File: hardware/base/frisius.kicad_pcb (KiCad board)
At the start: 4 copper layers, 46 x 85 mm, 123 parts, among them J1 MEM2067, J2 USB_C_Receptacle_USB2.0, J3 BATTERY, J4 Debug UART, J5 DISPLAY, J7 I2C ISENSE, Q2 Q_NMOS_DGS, Q3 Q_NMOS_DGS, SW1 RESET, SW2 BOOT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

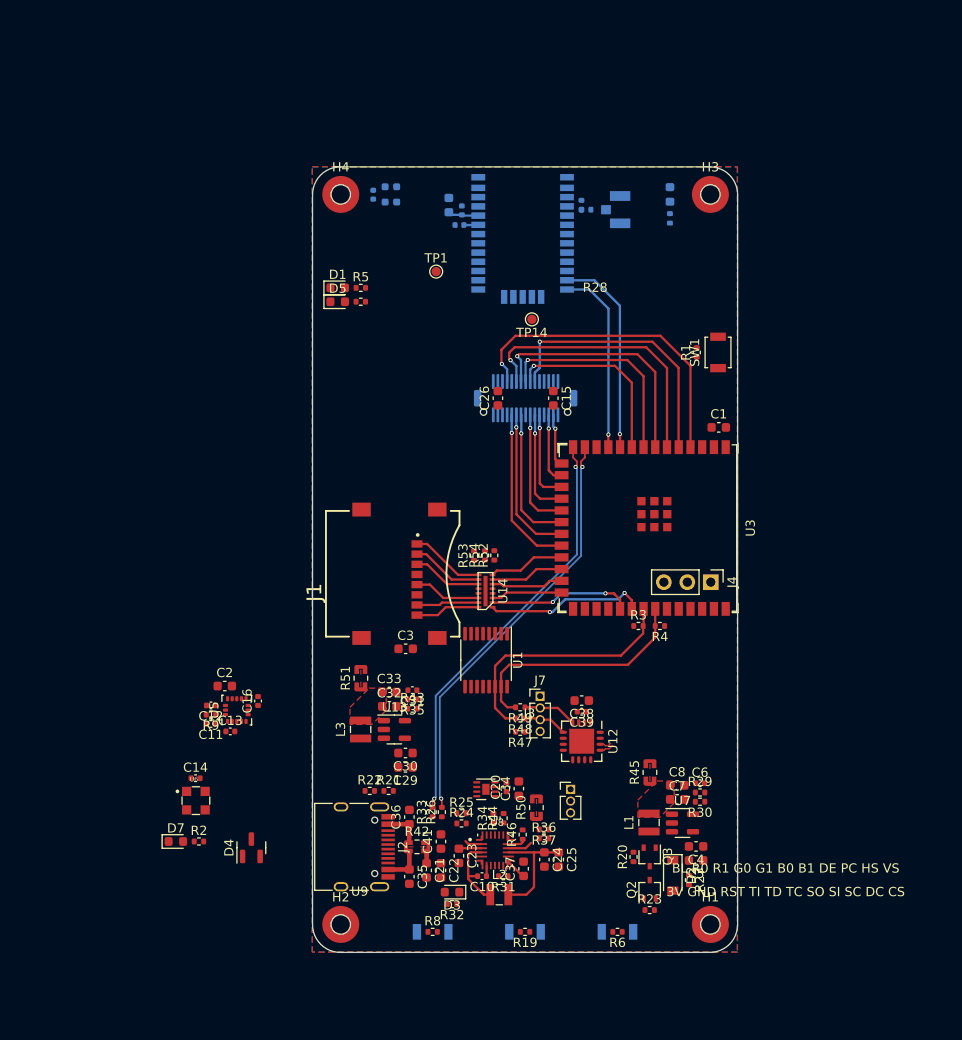
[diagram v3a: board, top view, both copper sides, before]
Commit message: more layout, optimising i2c
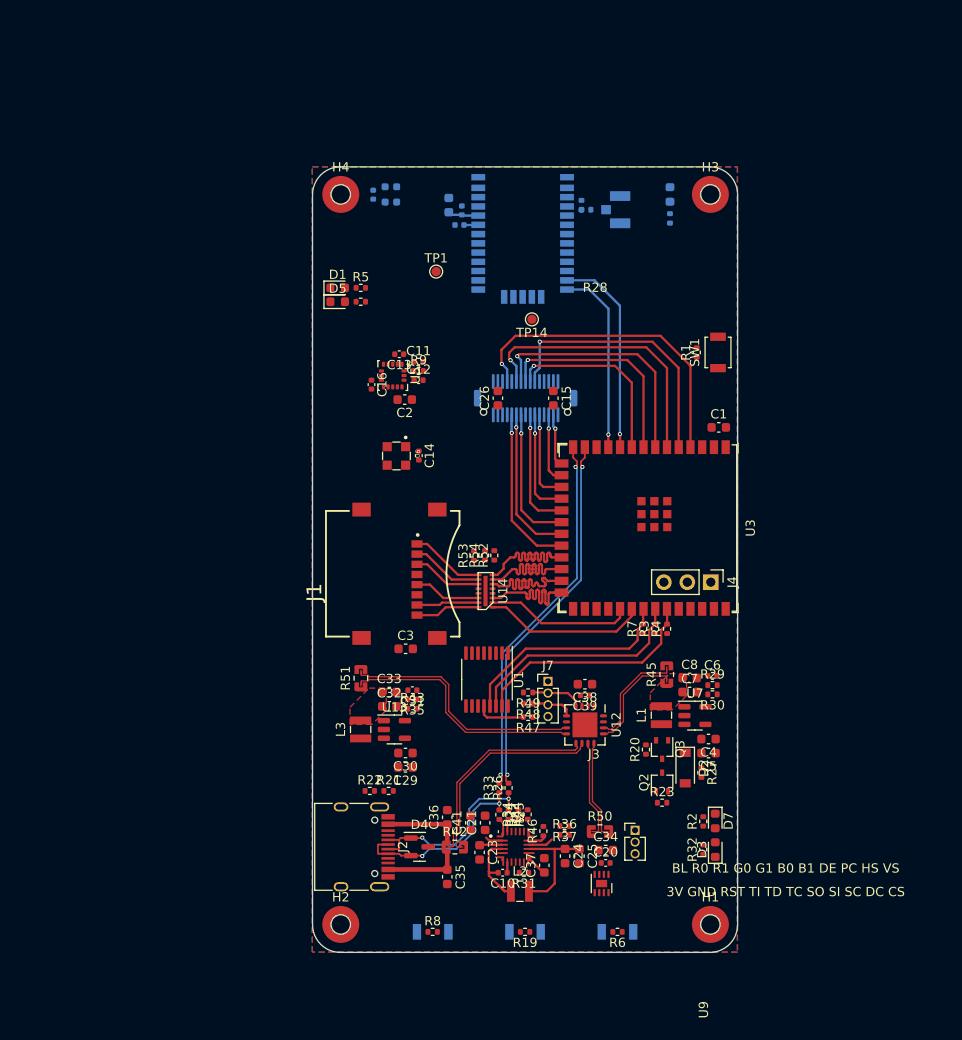
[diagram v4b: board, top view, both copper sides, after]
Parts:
- removed C22: 4.7u, Capacitor_SMD:C_0603_1608Metric
- added R7: 4.7k, Resistor_SMD:R_0402_1005Metric, F.Cu at (87.8, 95.0)
- moved D7 58.4 mm to (95.6, 115.8), turned to -90 degrees
- moved R2 54.6 mm to (94.3, 115.8), turned to 90 degrees
- moved C11 45.2 mm to (63.5, 66.1), turned to 0 degrees
- moved C13 44.7 mm to (61.4, 65.3), turned to 180 degrees
- moved R9 43.5 mm to (63.5, 67.1), turned to 0 degrees
- moved U6 43.2 mm to (61.1, 76.3), turned to -90 degrees
- moved C14 42.5 mm to (63.5, 76.3), turned to -90 degrees
- moved C12 41.8 mm to (63.5, 68.1), turned to 0 degrees
- moved U5 39.9 mm to (60.7, 67.6), turned to -90 degrees
- moved C2 36.6 mm to (62.0, 70.2), turned to 180 degrees
- moved C16 36.4 mm to (58.4, 68.6), turned to -90 degrees
- moved D3 28.9 mm to (95.6, 118.9), turned to 90 degrees
- moved R32 27.8 mm to (94.3, 118.9), turned to 90 degrees
- moved D4 18.2 mm to (63.6, 118.6), turned to 0 degrees
- moved U9 16.1 mm to (83.3, 122.6), turned to -90 degrees
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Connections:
- net Net-(C16-Pad1) renamed /Sensors/imu_crst
- net Net-(C35-Pad1) renamed /Power/vbus_port
- net Net-(D1-Pad2) renamed /GPS/1pps_led
- net Net-(D5-Pad2) renamed /GPS/3df_led
- net Net-(L1-Pad1) renamed /Power/core_drv
- net Net-(L3-Pad1) renamed /Power/aux_drv
- net Net-(R19-Pad1) renamed /Power/btn_nvdc
- C31 pad 1: Net-(C31-Pad1) -> /Power/aux_sw
- C32 pad 1: VDD_AUX_3V3 -> /Power/aux_sw
- C33 pad 1: VDD_AUX_3V3 -> /Power/aux_sw
- C6 pad 1: Net-(C6-Pad1) -> /Power/vcore_sw
- C7 pad 1: VDD_CORE_3V3 -> /Power/vcore_sw
- C8 pad 1: VDD_CORE_3V3 -> /Power/vcore_sw
- D4 pad 1: /Power/USB_D+ -> /Power/USB_D-
- D4 pad 2: /Power/USB_D- -> /Power/USB_D+
- L1 pad 2: Net-(C6-Pad1) -> /Power/vcore_sw
- L3 pad 2: Net-(C31-Pad1) -> /Power/aux_sw
- R29 pad 1: Net-(C6-Pad1) -> /Power/vcore_sw
- R35 pad 1: Net-(C31-Pad1) -> /Power/aux_sw
- R45 pad 1: Net-(C6-Pad1) -> /Power/vcore_sw
- R51 pad 1: Net-(C31-Pad1) -> /Power/aux_sw
- R51 pad 2: /Power/VAUX_S+ -> unconnected-(R51-Pad2)
- U1 pad 10: /Power/AUX_REG_EN -> /Power/BMS_INT
- U1 pad 9: /Power/BMS_INT -> /Power/AUX_REG_EN
- U12 pad 10: /Power/VBAT_S- -> /Power/VBUS_S-
- U12 pad 11: /Power/VCORE_S+ -> /Power/VBAT_S-
- U12 pad 12: /Power/VCORE_S- -> /Power/VBAT_S+
- U12 pad 13: /Power/VAUX_S+ -> /Power/VCORE_S+
- U12 pad 14: /Power/VAUX_S- -> /Power/VCORE_S-
- U12 pad 7: /Power/VBUS_S- -> /Power/VAUX_S-
- U12 pad 8: /Power/VBUS_S+ -> /Power/VAUX_S+
- U12 pad 9: /Power/VBAT_S+ -> /Power/VBUS_S+
- U3 pad 33: /Display/SYS_I2C.SDA -> /Processor/IOEXP_INT
- U3 pad 34: /Display/SYS_I2C.SCL -> /Display/SYS_I2C.SDA
- U3 pad 35: /Processor/IOEXP_INT -> /Display/SYS_I2C.SCL
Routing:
- net /Power/VAUX_S-: track 1.32 -> 26.8 mm
- net /Power/VAUX_S+: track 1.59 -> 26.8 mm
- net /Processor/IOEXP_INT: track 0.00 -> 24.1 mm
- net /Power/VBUS_S-: track 0.00 -> 22.8 mm
- net /Power/VBUS_S+: track 0.00 -> 22.8 mm
- net /Power/USB_D-: track 0.00 -> 20.9 mm, vias 0 -> 2
- net /Power/USB_D+: track 0.00 -> 20.9 mm, vias 0 -> 2
- net /Power/VCORE_S+: track 0.00 -> 11.6 mm
- net /Power/VCORE_S-: track 0.00 -> 11.6 mm
- net /Power/VBAT_S-: track 0.00 -> 10.5 mm
- net /Power/VBAT_S+: track 0.00 -> 10.5 mm
- net /Processor/SDMMC.D2: track 7.94 -> 16.2 mm
- net /Processor/SDMMC.CLK: track 7.71 -> 16.0 mm
- net /Power/vbus_port: track 8.59 -> 16.8 mm
- net /Processor/SDMMC.D3: track 8.25 -> 16.4 mm
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- added copper zone on F.Cu, net /Power/vcore_sw

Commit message: layout complete, drc checks and tweaks to silkscreen, attempting geo reannotate
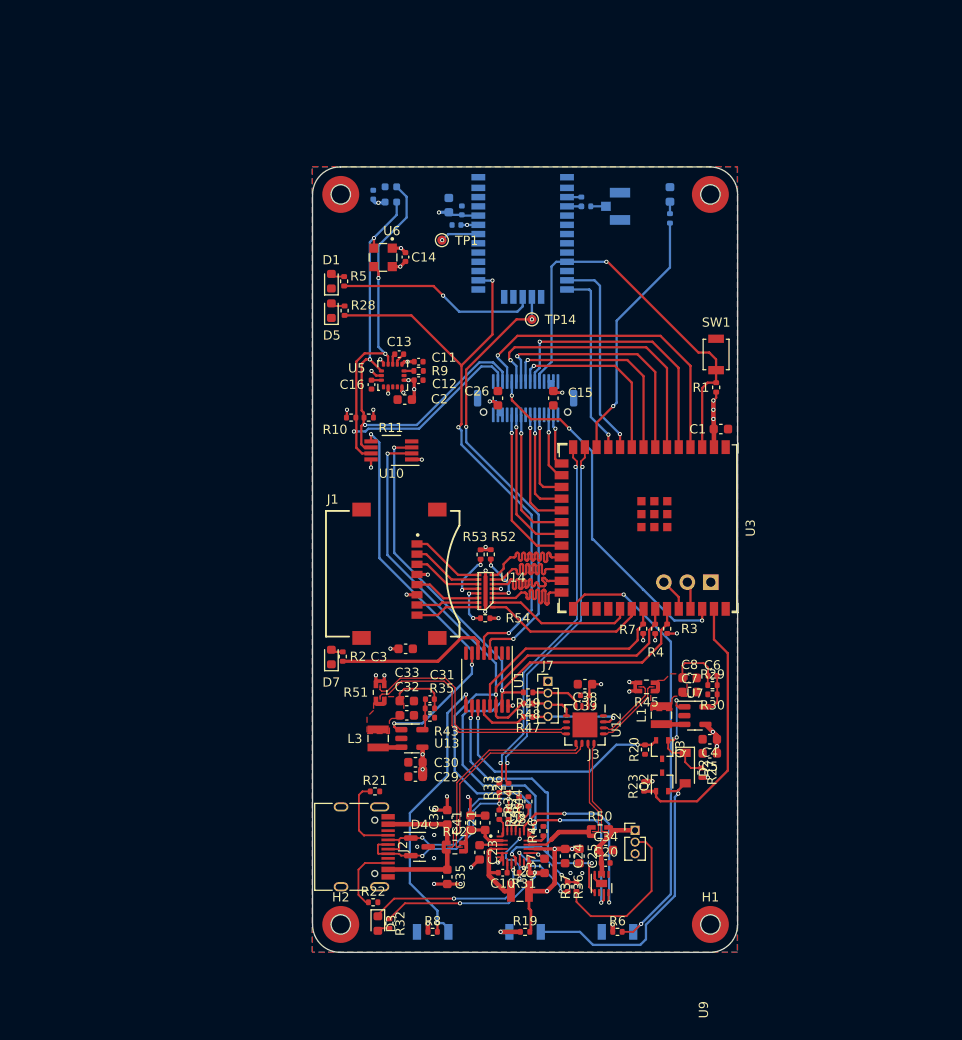
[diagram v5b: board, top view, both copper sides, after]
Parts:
- removed N6: Display Board, Symbol:WEEE-Logo_4.2x6mm_SilkScreen
- added R10: 4.7k, Resistor_SMD:R_0402_1005Metric, F.Cu at (56.2, 72.2)
- added R11: 4.7k, Resistor_SMD:R_0402_1005Metric, F.Cu at (58.1, 72.2)
- added U10: TCA9801, Package_SO:VSSOP-8_3.0x3.0mm_P0.65mm, F.Cu at (60.5, 75.7)
- H1: value BL -> TL
- H2: value BR -> BL
- H3: value TL -> TR
- H4: value TR -> BR
- J4: moved to B.Cu
- moved D7 45.2 mm to (54.1, 98.1), turned to 90 degrees
- moved R2 42.9 mm to (55.3, 98.0), turned to -90 degrees
- moved D3 37.4 mm to (59.1, 126.9), turned to -90 degrees
- moved R32 34.9 mm to (60.3, 126.9), turned to -90 degrees
- moved C14 21.5 mm to (62.1, 54.8)
- moved U6 21.5 mm to (59.6, 54.8)
- moved R22 12.1 mm to (58.6, 124.6)
- moved R54 6.80 mm to (70.7, 93.9), turned to 0 degrees
- moved R37 6.69 mm to (80.6, 122.9), turned to 90 degrees
- moved R36 5.63 mm to (79.6, 122.9), turned to -90 degrees
- moved R1 4.32 mm to (95.7, 68.9)
- moved TP1 3.46 mm to (66.0, 53.0)
- moved R23 2.62 mm to (87.9, 112.1), turned to 90 degrees
- moved R51 2.59 mm to (59.3, 101.9)
- moved R45 2.57 mm to (88.2, 101.3), turned to 180 degrees
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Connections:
- J5 pad 17: /Display/SYS_I2C.SCL -> /Display/AUX_I2C.SCL
- J5 pad 18: /Display/SYS_I2C.SDA -> /Display/AUX_I2C.SDA
- R3 pad 1: VDD_AUX_3V3 -> VDD_CORE_3V3
- R3 pad 2: /Display/SYS_I2C.SDA -> /Power/SYS_I2C.SCL
- R4 pad 1: VDD_AUX_3V3 -> VDD_CORE_3V3
- R4 pad 2: /Display/SYS_I2C.SCL -> /Power/SYS_I2C.SDA
- R47 pad 2: /Power/ISENSE_INT -> /Power/SYS_ISENSE_INT
- R48 pad 2: /Display/SYS_I2C.SDA -> /Power/SYS_I2C.SDA
- R49 pad 2: /Display/SYS_I2C.SCL -> /Power/SYS_I2C.SCL
- R51 pad 2: unconnected-(R51-Pad2) -> /Power/VAUX_S+
- R7 pad 1: VDD_AUX_3V3 -> VDD_CORE_3V3
- U1 pad 12: /Power/ISENSE_INT -> /Power/SYS_ISENSE_INT
- U1 pad 14: /Display/SYS_I2C.SDA -> /Power/SYS_I2C.SDA
- U1 pad 15: /Display/SYS_I2C.SCL -> /Power/SYS_I2C.SCL
- U1 pad 4: /GPS/GPS_FIX -> /GPS/GPS_FORCE_ON
- U1 pad 5: /GPS/GPS_FORCE_ON -> /GPS/GPS_FIX
- U1 pad 7: /Processor/NAV_BTN -> /Power/AUX_REG_EN
- U1 pad 9: /Power/AUX_REG_EN -> /Processor/NAV_BTN
- U2 pad 3: /Display/SYS_I2C.SCL -> /Display/AUX_I2C.SCL
- U2 pad 4: /Display/SYS_I2C.SDA -> /Display/AUX_I2C.SDA
- U3 pad 34: /Display/SYS_I2C.SDA -> /Power/SYS_I2C.SDA
- U3 pad 35: /Display/SYS_I2C.SCL -> /Power/SYS_I2C.SCL
- U5 pad 4: /Display/SYS_I2C.SCL -> /Display/AUX_I2C.SCL
- U5 pad 6: /Display/SYS_I2C.SDA -> /Display/AUX_I2C.SDA
- U6 pad 2: /Display/SYS_I2C.SDA -> /Display/AUX_I2C.SDA
- U6 pad 3: /Display/SYS_I2C.SCL -> /Display/AUX_I2C.SCL
- U8 pad 19-20: /Display/SYS_I2C.SCL -> /Power/SYS_I2C.SCL
- U8 pad 21: /Display/SYS_I2C.SDA -> /Power/SYS_I2C.SDA
- U9 pad 7: /Display/SYS_I2C.SCL -> /Power/SYS_I2C.SCL
- U9 pad 8: /Display/SYS_I2C.SDA -> /Power/SYS_I2C.SDA
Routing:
- net VDD_CORE_3V3: track 0.00 -> 133.4 mm, vias 0 -> 14
- net /Power/SYS_I2C.SDA: track 0.00 -> 106.7 mm, vias 0 -> 5
- net /Power/SYS_I2C.SCL: track 0.00 -> 103.6 mm, vias 0 -> 5
- net VDD_NVDC: track 13.4 -> 115.0 mm, vias 0 -> 9
- net /GPS/GPS_FIX: track 0.00 -> 65.0 mm, vias 0 -> 3
- net /Display/AUX_I2C.SCL: track 0.00 -> 57.5 mm, vias 0 -> 3
- net /Display/AUX_I2C.SDA: track 0.00 -> 51.6 mm, vias 0 -> 3
- net /GPS/GPS_FORCE_ON: track 0.00 -> 49.3 mm, vias 0 -> 3
- net /Processor/BOOT_BTN: track 0.00 -> 48.7 mm, vias 0 -> 2
- net ~{RESET}: track 0.00 -> 46.0 mm, vias 0 -> 1
- net /Power/AUX_REG_EN: track 0.00 -> 43.9 mm, vias 0 -> 3
- net /Display/DISPLAY_BL: track 0.00 -> 39.4 mm, vias 0 -> 3
- net /Power/BMS_INT: track 0.00 -> 36.8 mm, vias 0 -> 3
- net /Processor/NAV_BTN: track 0.00 -> 32.1 mm, vias 0 -> 2
- net /Power/BOOTSTRAP: track 0.00 -> 32.0 mm, vias 0 -> 1
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- added copper zone on F.Cu, net /Power/aux_sw
- added copper zone on In2.Cu, net VDD_AUX_3V3
- added copper zone on In2.Cu, net VDD_CORE_3V3
- added copper zone on In2.Cu, net VDD_NVDC
- removed copper zone on F.Cu, net VDD_AUX_3V3
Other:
- board text removed: "3V GND RST TI TD TC SO SI SC DC CS"
- board text removed: "BL R0 R1 G0 G1 B0 B1 DE PC HS VS"

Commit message: Tidied up, added more stitches
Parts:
- added TP2: GPS_FON, TestPoint:TestPoint_Pad_D1.0mm, F.Cu at (83.8, 55.3)
- U10: value TCA9801 -> TCA9803
- moved U3 0.35 mm to (88.1, 84.1)
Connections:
- U10 pad 4: unconnected-(U10-Pad4) -> GND
- U4 pad 23: ~{RESET} -> /GPS/GPS_RESET
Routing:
- net ~{RESET}: track 46.0 -> 36.3 mm
- net /GPS/GPS_RESET: track 0.00 -> 4.40 mm, vias 0 -> 1
- net GND: track 27.4 -> 29.0 mm, vias 21 -> 236
- net /Power/USB_ESP.D+: track 40.3 -> 41.5 mm
- net /Processor/BOOT_BTN: track 48.7 -> 49.6 mm
- net /Processor/DEBUG_TX: track 2.55 -> 1.85 mm
- net /Power/USB_ESP.D-: track 40.3 -> 40.9 mm
- net /Display/LCD_RGB.B0: track 6.99 -> 7.56 mm
- net /Power/aux_sw: track 6.60 -> 7.10 mm
- added copper zone on F.Cu, net /Power/chg_sw
- added copper zone on F.Cu, net VDD_NVDC
